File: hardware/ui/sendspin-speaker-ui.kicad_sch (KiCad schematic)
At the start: 0 parts

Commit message: hardware: front panel and USB-C board schematics; docs
All three projects pass ERC with 0 violations and every part has its
footprint. Open checks (PJ-320D pinout, NS4150B values) in the README.

Co-Authored-By: Claude Opus 5.5 <noreply@anthropic.com>
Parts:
- added C601: 100n, Capacitor_SMD:C_0805_2012Metric, symbol Device:C
- added C602: 1u, Capacitor_SMD:C_0805_2012Metric, symbol Device:C
- added D601: status, LED_SMD:LED_0805_2012Metric, symbol Device:LED
- added J601: J_UI, Connector_JST:JST_XH_B12B-XH-A_1x12_P2.50mm_Vertical, symbol Connector_Generic:Conn_01x12
- added J602: SPI display, Connector_PinHeader_2.54mm:PinHeader_1x08_P2.54mm_Vertical, symbol Connector_Generic:Conn_01x08
- added J603: I2C OLED, Connector_PinHeader_2.54mm:PinHeader_1x04_P2.54mm_Vertical, symbol Connector_Generic:Conn_01x04
- added R601: 10k, Resistor_SMD:R_0805_2012Metric, symbol Device:R
- added R602: 1k, Resistor_SMD:R_0805_2012Metric, symbol Device:R
- added SW601: Play/Pause, Button_Switch_THT:SW_PUSH_6mm, symbol Switch:SW_Push
- added SW603: Prev, Button_Switch_THT:SW_PUSH_6mm, symbol Switch:SW_Push
- added SW604: Next, Button_Switch_THT:SW_PUSH_6mm, symbol Switch:SW_Push
- added SW605: Vol -, Button_Switch_THT:SW_PUSH_6mm, symbol Switch:SW_Push
- added SW606: Vol +, Button_Switch_THT:SW_PUSH_6mm, symbol Switch:SW_Push
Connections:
- new net +3V3: C601.1, J601.1 (Pin_1), J602.1 (Pin_1), J602.8 (Pin_8), J603.2 (Pin_2), R601.1
- new net BTN1: J601.7 (Pin_7), SW601.1
- new net BTN3: J601.8 (Pin_8), SW603.1
- new net BTN4: J601.9 (Pin_9), SW604.1
- new net BTN5: J601.10 (Pin_10), SW605.1
- new net BTN6: J601.11 (Pin_11), SW606.1
- new net DISP_CS: J601.5 (Pin_5), J602.5 (Pin_5)
- new net DISP_DC: J601.6 (Pin_6), J602.6 (Pin_6)
- new net DISP_MOSI: J601.4 (Pin_4), J602.3 (Pin_3), J603.4 (Pin_4)
- new net DISP_RST: C602.1, J602.7 (Pin_7), R601.2
- new net DISP_SCK: J601.3 (Pin_3), J602.4 (Pin_4), J603.3 (Pin_3)
- new net GND: C601.2, C602.2, D601.1 (K), J601.2 (Pin_2), J602.2 (Pin_2), J603.1 (Pin_1), SW601.2, SW603.2, SW604.2, SW605.2, SW606.2
- new net LED: J601.12 (Pin_12), R602.1
- new net LED_A: D601.2 (A), R602.2
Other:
- note added: "Front panel Fit J602 for the SPI ST7789 (as on the Audio Kit build) or J603 for an I2C OLED (then fit R105/R106 on the main board). Check the module's pin order before soldering: OLED modules come as GND-VCC-SCL-SDA and VCC-GND-SCL-SDA. ST7789 reset: R601/C602 RC at power-up (the firmware has no reset pin). Backlight always on. Buttons pull to GND; BTN1 (GPIO36) has its 10k pull-up on the main bo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"

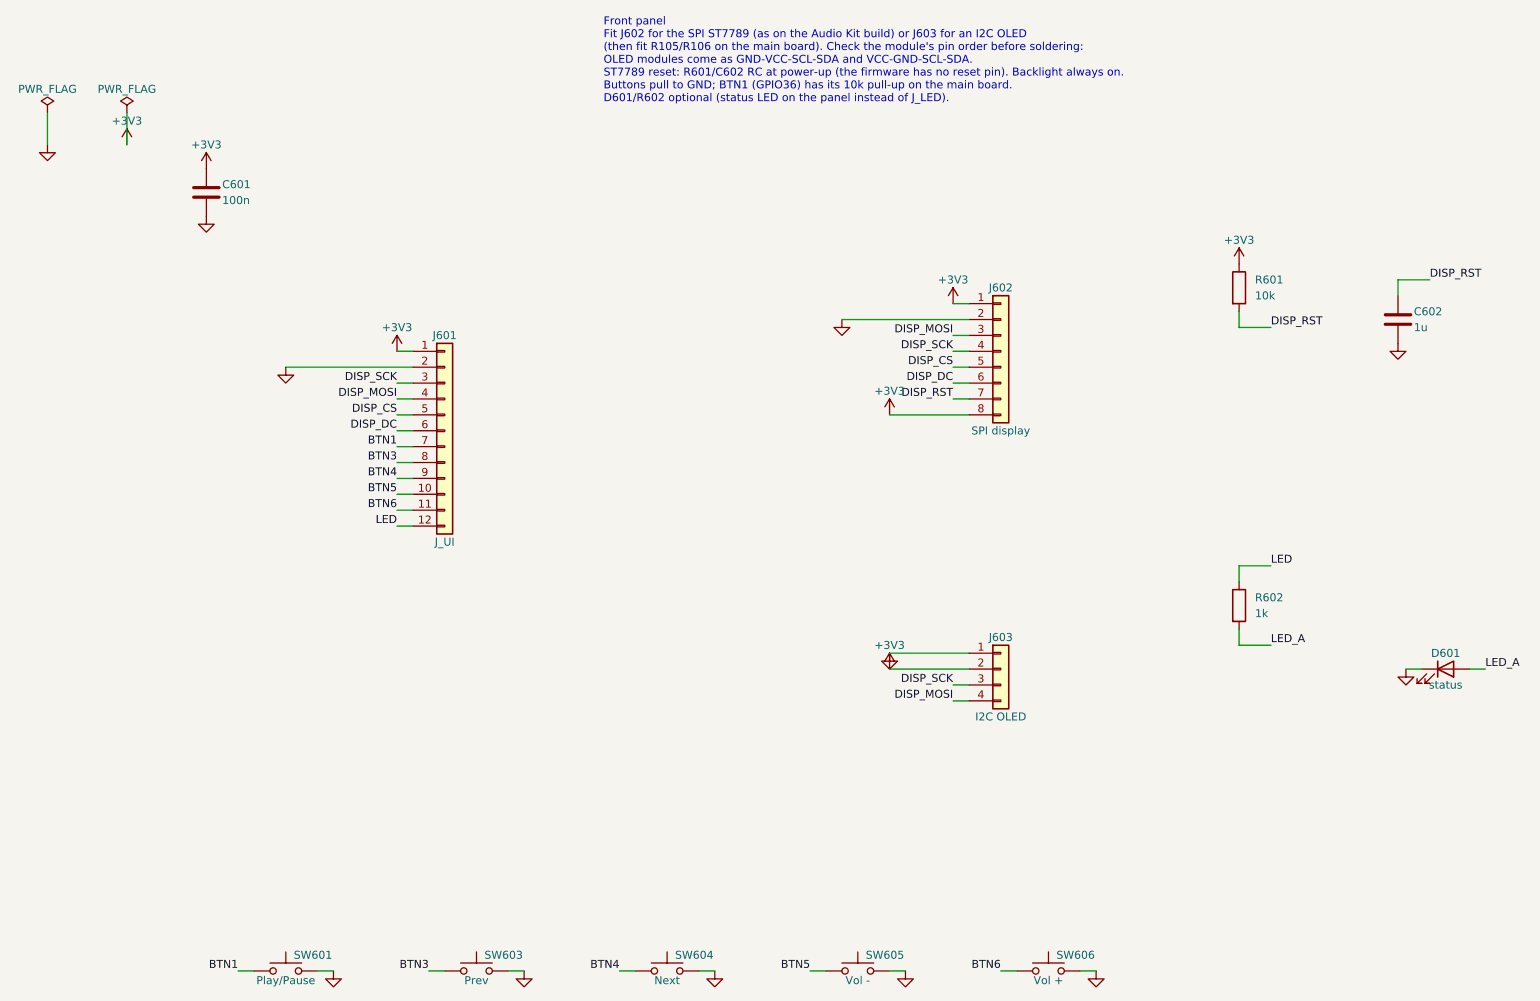
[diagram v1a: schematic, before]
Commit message: hardware: bare USB-C board and front panel (schematics)
J_USB carries CC1/CC2 (XH 6); CC resistors and ESD stay on the main
board. Front panel has only buttons and headers; its LED pin comes
through R501. Boards not yet updated from the schematics.

Co-Authored-By: Claude Opus 5.5 <noreply@anthropic.com>
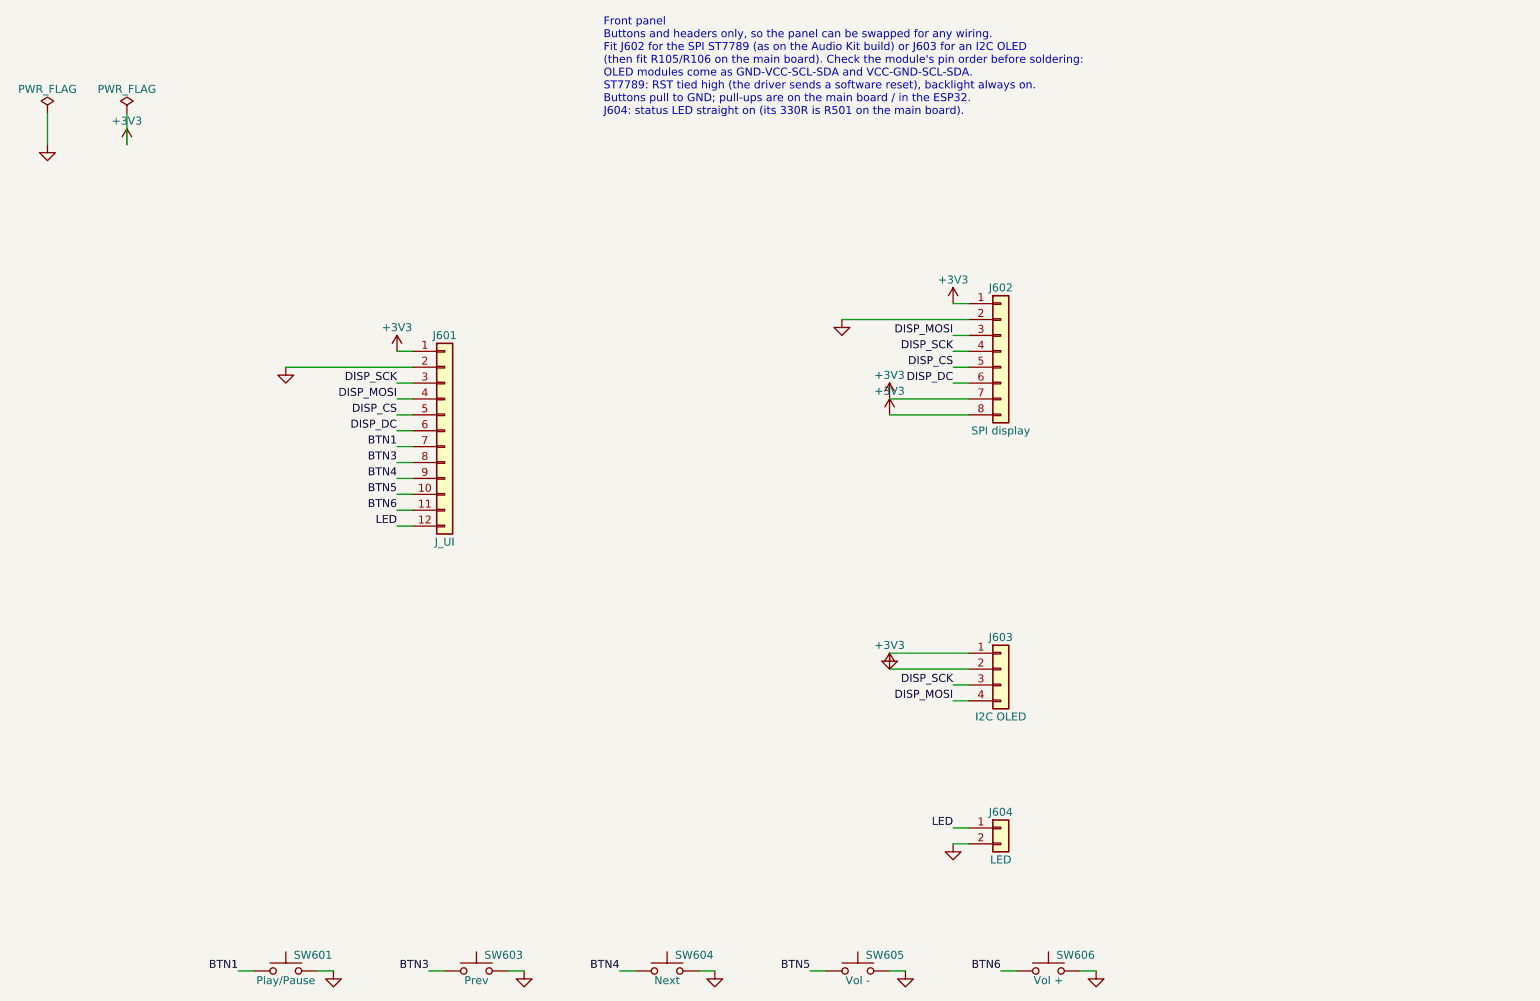
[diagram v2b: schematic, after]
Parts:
- removed C601: 100n, Capacitor_SMD:C_0805_2012Metric, symbol Device:C
- removed C602: 1u, Capacitor_SMD:C_0805_2012Metric, symbol Device:C
- removed D601: status, LED_SMD:LED_0805_2012Metric, symbol Device:LED
- removed R601: 10k, Resistor_SMD:R_0805_2012Metric, symbol Device:R
- removed R602: 1k, Resistor_SMD:R_0805_2012Metric, symbol Device:R
- added J604: LED, Connector_PinHeader_2.54mm:PinHeader_1x02_P2.54mm_Vertical, symbol Connector_Generic:Conn_01x02
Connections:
- net DISP_RST is gone; now on net +3V3: J602.7 (Pin_7)
- net GND: now also J604.2 (Pin_2)
- net LED: now also J604.1 (Pin_1)
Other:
- note added: "Front panel Buttons and headers only, so the panel can be swapped for any wiring. Fit J602 for the SPI ST7789 (as on the Audio Kit build) or J603 for an I2C OLED (then fit R105/R106 on the main board). Check the module's pin order before soldering: OLED modules come as GND-VCC-SCL-SDA and VCC-GND-SCL-SDA. ST7789: RST tied high (the driver sends a software reset), backlight always on. Buttons pull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"
- note removed: "Front panel Fit J602 for the SPI ST7789 (as on the Audio Kit build) or J603 for an I2C OLED (then fit R105/R106 on the main board). Check the module's pin order before soldering: OLED modules come as GND-VCC-SCL-SDA and VCC-GND-SCL-SDA. ST7789 reset: R601/C602 RC at power-up (the firmware has no reset pin). Backlight always on. Buttons pull to GND; BTN1 (GPIO36) has its 10k pull-up on the main bo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"
